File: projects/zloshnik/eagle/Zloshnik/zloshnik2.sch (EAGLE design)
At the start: 104 parts, among them IC1 TL5626D, IC2 78L05F, IC6 DS3234, IC7 MEGA8-AI, Q2 IRF630N, Q4 IRF630N, SW1 BUTTON-IT_1181

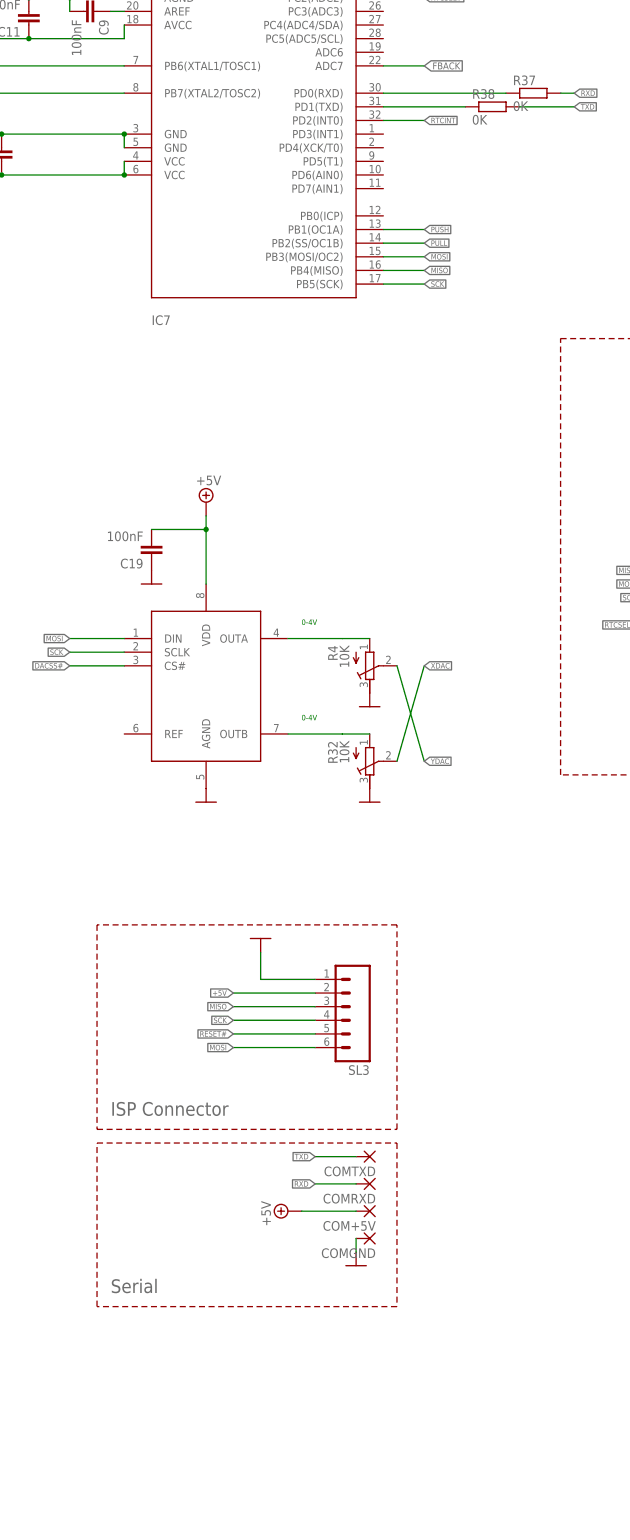
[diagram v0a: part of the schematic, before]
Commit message: +3v3 and conversion for bluetooth, more sparse layout in hv area
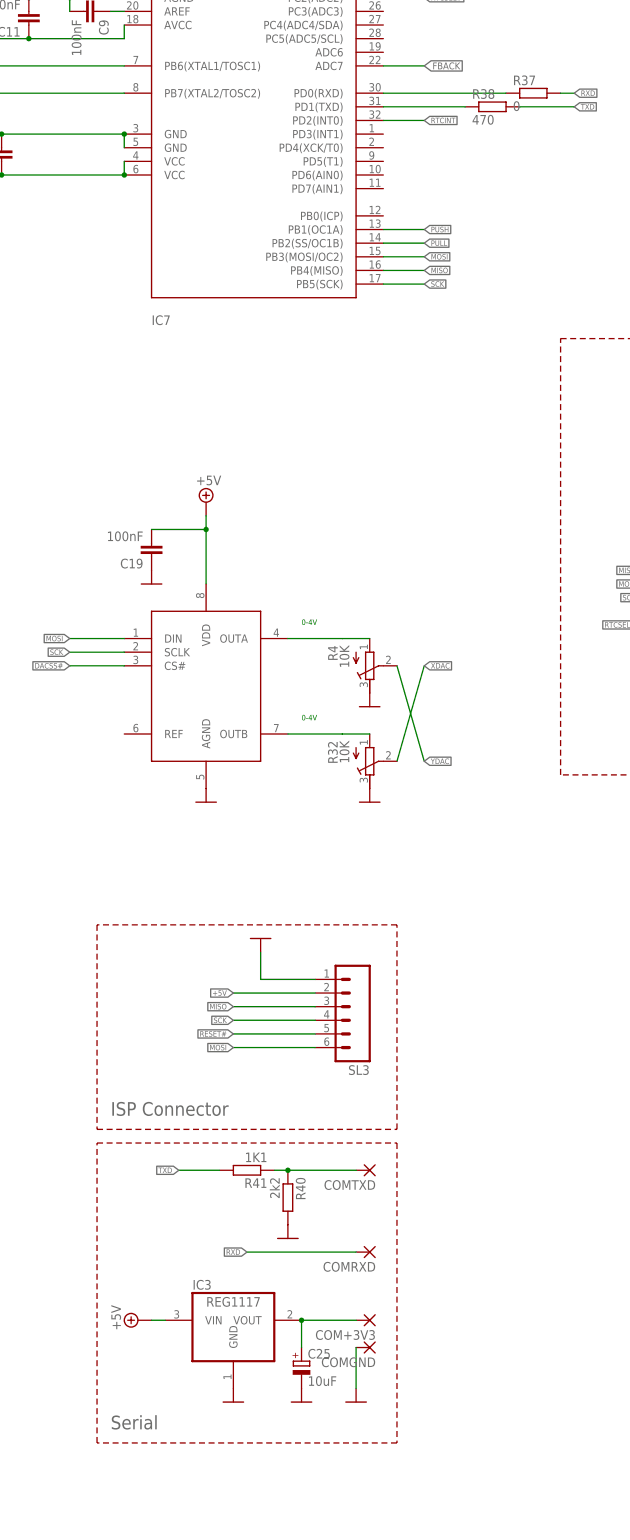
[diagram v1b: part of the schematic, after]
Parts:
- removed COM+5V: (no value), wirepad:1,6/0,8
- added C25: 10uF, rcl:CPOL-EUSMCB
- added COM+3V3: (no value), wirepad:1,6/0,8
- added IC3: REG1117, burr-brown:REG1117
- added R40: 2k2, rcl:R-EU_R0805S
- added R41: 1K1, rcl:R-EU_R0805S
- R37: value 0K -> 0; device rcl:R-EU_R1206 -> 0-rcl:R-EU_R1206
- R38: value 0K -> 470; device rcl:R-EU_R1206 -> 0-rcl:R-EU_R1206
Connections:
- new net +3V3: C25.+, COM+3V3.P, IC3.VOUT
- new net N$3: COMTXD.P, R40.1, R41.1
- net +5V: now also IC3.VIN; no longer COM+5V.P
- net GND: now also C25.-, IC3.GND, R40.2
- net TXD: now also R41.2; no longer COMTXD.P
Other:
- moved on the sheet: COMGND, COMRXD, COMTXD

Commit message: lots of fixes
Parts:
- removed BAT+, BAT-: (no value), wirepad:1,6/0,8
- removed R41: 1K1, rcl:R-EU_R0805S
- added CAP+, CAP-: (no value), wirepad:2,54/0,8
- added HEA1, HEA2: (no value), wirepad:1,6/0,8
- C23: value 0,01 1kV -> 0,1 1kV
- R34: value 100K -> 75-100K
- R37: device 0-rcl:R-EU_R1206 -> rcl:R-EU_R0805S
- R38: value 470 -> 1K; device 0-rcl:R-EU_R1206 -> rcl:R-EU_R0805S
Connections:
- net N$36 renamed ZDACN$36
- removed net N$15: R10.A, R11.2
- removed net N$3: COMTXD.P, R40.1, R41.1
- new net N$12: R10.E, R11.2
- net -450V: now also R10.A; no longer R10.E
- net GND: now also CAP-.P; no longer BAT-.P
- net HEATERA: now also HEA1.P
- net HEATERB: now also HEA2.P
- net N$5: now also CAP+.P; no longer BAT+.P
- net TXD: now also COMTXD.P, R40.1; no longer R41.2
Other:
- moved on the sheet: R10

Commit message: stuff
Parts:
- added R39: TRIMPOTSMD, SparkFun:TRIMPOTSMD
- added R41: TRIMPOT3MM-2, SparkFun:TRIMPOT3MM-2
- added R42: TRIMPOT-2, SparkFun:TRIMPOT-2
- added R47: (no value), 0-rcl:R-TRIMMTS63Z
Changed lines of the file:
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@@
 <grid distance="0.1" unitdist="inch" unit="inch" style="lines" multiple="1" display="no" altdistance="0.01" altunitdist="inch" altunit="inch"/>
 <layers>
-<layer number="1" name="Top" color="4" fill="1" visible="yes" active="no"/>
-<layer number="16" name="Bottom" color="1" fill="1" visible="yes" active="no"/>
-<layer number="17" name="Pads" color="2" fill="1" visible="yes" active="no"/>
-<layer number="18" name="Vias" color="2" fill="1" visible="yes" active="no"/>
-<layer number="19" name="Unrouted" color="6" fill="1" visible="yes" active="no"/>
-<layer number="20" name="Dimension" color="15" fill="1" visible="yes" active="no"/>
-<layer number="21" name="tPlace" color="7" fill="1" visible="yes" active="no"/>
-<layer number="22" name="bPlace" color="7" fill="1" visible="yes" active="no"/>
-<layer number="23" name="tOrigins" color="15" fill="1" visible="yes" active="no"/>
-<layer number="24" name="bOrigins" color="15" fill="1" visible="yes" active="no"/>
-<layer number="25" name="tNames" color="7" fill="1" visible="yes" active="no"/>
-<layer number="26" name="bNames" color="7" fill="1" visible="yes" active="no"/>
-<layer number="27" name="tValues" color="7" fill="1" visible="yes" active="no"/>
-<layer number="28" name="bValues" color="7" fill="1" visible="yes" active="no"/>
+<layer number="1" name="Top" color="4" fill="1" visible="no" active="no"/>
+<layer number="16" name="Bottom" color="1" fill="1" visible="no" active="no"/>
+<layer number="17" name="Pads" color="2" fill="1" visible="no" active="no"/>
+<layer number="18" name="Vias" color="2" fill="1" visible="no" active="no"/>
+<layer number="19" name="Unrouted" color="6" fill="1" visible="no" active="no"/>
+<layer number="20" name="Dimension" color="15" fill="1" visible="no" active="no"/>
+<layer number="21" name="tPlace" color="7" fill="1" visible="no" active="no"/>
+<layer number="22" name="bPlace" color="7" fill="1" visible="no" active="no"/>
+<layer number="23" name="tOrigins" color="15" fill="1" visible="no" active="no"/>
+<layer number="24" name="bOrigins" color="15" fill="1" visible="no" active="no"/>
+<layer number="25" name="tNames" color="7" fill="1" visible="no" active="no"/>
+<layer number="26" name="bNames" color="7" fill="1" visible="no" active="no"/>
+<layer number="27" name="tValues" color="7" fill="1" visible="no" active="no"/>
+<layer number="28" name="bValues" color="7" fill="1" visible="no" active="no"/>
 <layer number="29" name="tStop" color="7" fill="3" visible="no" active="no"/>
 <layer number="30" name="bStop" color="7" fill="6" visible="no" active="no"/>
@@
 <layer number="35" name="tGlue" color="7" fill="4" visible="no" active="no"/>
 <layer number="36" name="bGlue" color="7" fill="5" visible="no" active="no"/>
-<layer number="37" name="tTest" color="7" fill="1" visible="yes" active="no"/>
-<layer number="38" name="bTest" color="7" fill="1" visible="yes" active="no"/>
+<layer number="37" name="tTest" color="7" fill="1" visible="no" active="no"/>
+<layer number="38" name="bTest" color="7" fill="1" visible="no" active="no"/>
 <layer number="39" name="tKeepout" color="4" fill="11" visible="no" active="no"/>
 <layer number="40" name="bKeepout" color="1" fill="11" visible="no" active="no"/>
@@
 <layer number="44" name="Drills" color="7" fill="1" visible="no" active="no"/>
 <layer number="45" name="Holes" color="7" fill="1" visible="no" active="no"/>
-<layer number="46" name="Milling" color="3" fill="1" visible="yes" active="no"/>
-<layer number="47" name="Measures" color="7" fill="1" visible="yes" active="no"/>
-<layer number="48" name="Document" color="7" fill="1" visible="yes" active="no"/>
-<layer number="49" name="Reference" color="7" fill="1" visible="yes" active="no"/>
-<layer number="50" name="dxf" color="7" fill="1" visible="yes" active="no"/>
-<layer number="51" name="tDocu" color="7" fill="1" visible="yes" active="no"/>
-<layer number="52" name="bDocu" color="7" fill="1" visible="yes" active="no"/>
-<layer number="53" name="tGND_GNDA" color="7" fill="9" visible="yes" active="no"/>
-<layer number="54" name="bGND_GNDA" color="1" fill="9" visible="yes" active="no"/>
-<layer number="56" name="wert" color="7" fill="1" visible="yes" active="no"/>
+<layer number="46" name="Milling" color="3" fill="1" visible="no" active="no"/>
+<layer number="47" name="Measures" color="7" fill="1" visible="no" active="no"/>
+<layer number="48" name="Document" color="7" fill="1" visible="no" active="no"/>
+<layer number="49" name="Reference" color="7" fill="1" visible="no" active="no"/>
+<layer number="50" name="dxf" color="7" fill="1" visible="no" active="no"/>
+<layer number="51" name="tDocu" color="7" fill="1" visible="no" active="no"/>
+<layer number="52" name="bDocu" color="7" fill="1" visible="no" active="no"/>
+<layer number="53" name="tGND_GNDA" color="7" fill="9" visible="no" active="no"/>
+<layer number="54" name="bGND_GNDA" color="1" fill="9" visible="no" active="no"/>
+<layer number="56" name="wert" color="7" fill="1" visible="no" active="no"/>
 <layer number="91" name="Nets" color="2" fill="1" visible="yes" active="yes"/>
 <layer number="92" name="Busses" color="1" fill="1" visible="yes" active="yes"/>
@@
 <part name="CAP-" library="wirepad" deviceset="2,54/0,8" device=""/>
 <part name="CAP+" library="wirepad" deviceset="2,54/0,8" device=""/>
+<part name="R39" library="SparkFun" deviceset="TRIMPOT" device="SMD"/>
+<part name="R41" library="SparkFun" deviceset="TRIMPOT" device="3MM-2"/>
+<part name="R42" library="SparkFun" deviceset="TRIMPOT" device="-2"/>
+<part name="R47" library="0-rcl" deviceset="R-TRIMM" device="TS63Z"/>
 </parts>
 <sheets>
@@
 <instance part="CAP-" gate="P" x="678.18" y="142.24" rot="R270"/>
 <instance part="CAP+" gate="P" x="670.56" y="142.24" rot="R270"/>
+<instance part="R39" gate="R?" x="246.38" y="99.06"/>
+<instance part="R41" gate="R?" x="246.38" y="86.36"/>
+<instance part="R42" gate="R?" x="246.38" y="71.12"/>
+<instance part="R47" gate="G$1" x="190.5" y="68.58"/>
 </instances>
 <busses>
@@
 </segment>
 </net>
-<net name="N$34" class="0">
+<net name="N$34" class="3">
 <segment>
 <pinref part="R33" gate="G$1" pin="2"/>

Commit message: just updated the board
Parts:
- removed R41: TRIMPOT3MM-2, SparkFun:TRIMPOT3MM-2
- removed R42: TRIMPOT-2, SparkFun:TRIMPOT-2
- R39: value TRIMPOTSMD -> (none); device SparkFun:TRIMPOTSMD -> 0-rcl:R-TRIMM3314J
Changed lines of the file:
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@@
 <grid distance="0.1" unitdist="inch" unit="inch" style="lines" multiple="1" display="no" altdistance="0.01" altunitdist="inch" altunit="inch"/>
 <layers>
-<layer number="1" name="Top" color="4" fill="1" visible="no" active="no"/>
-<layer number="16" name="Bottom" color="1" fill="1" visible="no" active="no"/>
-<layer number="17" name="Pads" color="2" fill="1" visible="no" active="no"/>
-<layer number="18" name="Vias" color="2" fill="1" visible="no" active="no"/>
-<layer number="19" name="Unrouted" color="6" fill="1" visible="no" active="no"/>
-<layer number="20" name="Dimension" color="15" fill="1" visible="no" active="no"/>
-<layer number="21" name="tPlace" color="7" fill="1" visible="no" active="no"/>
-<layer number="22" name="bPlace" color="7" fill="1" visible="no" active="no"/>
-<layer number="23" name="tOrigins" color="15" fill="1" visible="no" active="no"/>
-<layer number="24" name="bOrigins" color="15" fill="1" visible="no" active="no"/>
-<layer number="25" name="tNames" color="7" fill="1" visible="no" active="no"/>
-<layer number="26" name="bNames" color="7" fill="1" visible="no" active="no"/>
-<layer number="27" name="tValues" color="7" fill="1" visible="no" active="no"/>
-<layer number="28" name="bValues" color="7" fill="1" visible="no" active="no"/>
+<layer number="1" name="Top" color="4" fill="1" visible="yes" active="no"/>
+<layer number="16" name="Bottom" color="1" fill="1" visible="yes" active="no"/>
+<layer number="17" name="Pads" color="2" fill="1" visible="yes" active="no"/>
+<layer number="18" name="Vias" color="2" fill="1" visible="yes" active="no"/>
+<layer number="19" name="Unrouted" color="6" fill="1" visible="yes" active="no"/>
+<layer number="20" name="Dimension" color="15" fill="1" visible="yes" active="no"/>
+<layer number="21" name="tPlace" color="7" fill="1" visible="yes" active="no"/>
+<layer number="22" name="bPlace" color="7" fill="1" visible="yes" active="no"/>
+<layer number="23" name="tOrigins" color="15" fill="1" visible="yes" active="no"/>
+<layer number="24" name="bOrigins" color="15" fill="1" visible="yes" active="no"/>
+<layer number="25" name="tNames" color="7" fill="1" visible="yes" active="no"/>
+<layer number="26" name="bNames" color="7" fill="1" visible="yes" active="no"/>
+<layer number="27" name="tValues" color="7" fill="1" visible="yes" active="no"/>
+<layer number="28" name="bValues" color="7" fill="1" visible="yes" active="no"/>
 <layer number="29" name="tStop" color="7" fill="3" visible="no" active="no"/>
 <layer number="30" name="bStop" color="7" fill="6" visible="no" active="no"/>
@@
 <layer number="35" name="tGlue" color="7" fill="4" visible="no" active="no"/>
 <layer number="36" name="bGlue" color="7" fill="5" visible="no" active="no"/>
-<layer number="37" name="tTest" color="7" fill="1" visible="no" active="no"/>
-<layer number="38" name="bTest" color="7" fill="1" visible="no" active="no"/>
+<layer number="37" name="tTest" color="7" fill="1" visible="yes" active="no"/>
+<layer number="38" name="bTest" color="7" fill="1" visible="yes" active="no"/>
 <layer number="39" name="tKeepout" color="4" fill="11" visible="no" active="no"/>
 <layer number="40" name="bKeepout" color="1" fill="11" visible="no" active="no"/>
@@
 <layer number="44" name="Drills" color="7" fill="1" visible="no" active="no"/>
 <layer number="45" name="Holes" color="7" fill="1" visible="no" active="no"/>
-<layer number="46" name="Milling" color="3" fill="1" visible="no" active="no"/>
-<layer number="47" name="Measures" color="7" fill="1" visible="no" active="no"/>
-<layer number="48" name="Document" color="7" fill="1" visible="no" active="no"/>
-<layer number="49" name="Reference" color="7" fill="1" visible="no" active="no"/>
-<layer number="50" name="dxf" color="7" fill="1" visible="no" active="no"/>
-<layer number="51" name="tDocu" color="7" fill="1" visible="no" active="no"/>
-<layer number="52" name="bDocu" color="7" fill="1" visible="no" active="no"/>
-<layer number="53" name="tGND_GNDA" color="7" fill="9" visible="no" active="no"/>
-<layer number="54" name="bGND_GNDA" color="1" fill="9" visible="no" active="no"/>
-<layer number="56" name="wert" color="7" fill="1" visible="no" active="no"/>
+<layer number="46" name="Milling" color="3" fill="1" visible="yes" active="no"/>
+<layer number="47" name="Measures" color="7" fill="1" visible="yes" active="no"/>
+<layer number="48" name="Document" color="7" fill="1" visible="yes" active="no"/>
+<layer number="49" name="Reference" color="7" fill="1" visible="yes" active="no"/>
+<layer number="50" name="dxf" color="7" fill="1" visible="yes" active="no"/>
+<layer number="51" name="tDocu" color="7" fill="1" visible="yes" active="no"/>
+<layer number="52" name="bDocu" color="7" fill="1" visible="yes" active="no"/>
+<layer number="53" name="tGND_GNDA" color="7" fill="9" visible="yes" active="no"/>
+<layer number="54" name="bGND_GNDA" color="1" fill="9" visible="yes" active="no"/>
+<layer number="56" name="wert" color="7" fill="1" visible="yes" active="no"/>
 <layer number="91" name="Nets" color="2" fill="1" visible="yes" active="yes"/>
 <layer number="92" name="Busses" color="1" fill="1" visible="yes" active="yes"/>
@@
 <part name="CAP-" library="wirepad" deviceset="2,54/0,8" device=""/>
 <part name="CAP+" library="wirepad" deviceset="2,54/0,8" device=""/>
-<part name="R39" library="SparkFun" deviceset="TRIMPOT" device="SMD"/>
-<part name="R41" library="SparkFun" deviceset="TRIMPOT" device="3MM-2"/>
-<part name="R42" library="SparkFun" deviceset="TRIMPOT" device="-2"/>
 <part name="R47" library="0-rcl" deviceset="R-TRIMM" device="TS63Z"/>
+<part name="R39" library="0-rcl" deviceset="R-TRIMM" device="3314J"/>
 </parts>
 <sheets>
@@
 <instance part="CAP-" gate="P" x="678.18" y="142.24" rot="R270"/>
 <instance part="CAP+" gate="P" x="670.56" y="142.24" rot="R270"/>
-<instance part="R39" gate="R?" x="246.38" y="99.06"/>
-<instance part="R41" gate="R?" x="246.38" y="86.36"/>
-<instance part="R42" gate="R?" x="246.38" y="71.12"/>
 <instance part="R47" gate="G$1" x="190.5" y="68.58"/>
+<instance part="R39" gate="G$1" x="190.5" y="83.82"/>
 </instances>
 <busses>
